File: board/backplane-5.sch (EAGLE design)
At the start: 142 parts, among them CN1 RJ45JACK90, U1 AMS1117-5.0, U10 RT9193, U11 KSZ9897, U12 KSZ8081MLX, U2 AMS1117-5.0, U3 AMS1117-5.0, U4 AMS1117-5.0, U5 AMS1117-5.0, U6 AMS1117-2.5, U7 AMS1117-1.2, U8 RT9193, U9 AMS1117-5.0, X1 25MHz, X2 25MHz

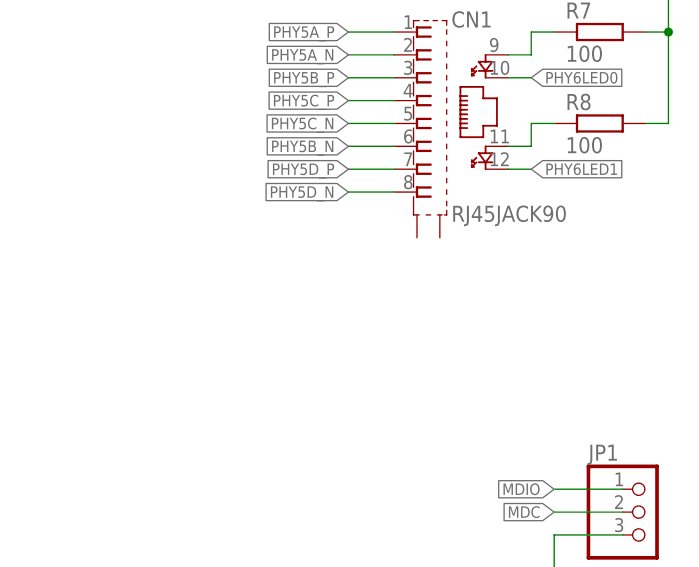
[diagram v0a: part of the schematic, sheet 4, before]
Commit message: Tweaked some packages and placed RPi conn
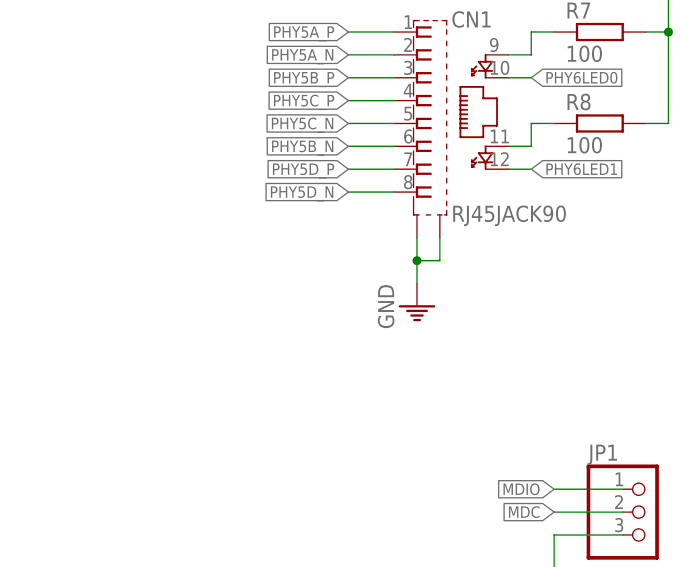
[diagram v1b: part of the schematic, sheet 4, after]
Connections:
- net PE: now also CN1.S1, CN1.S2
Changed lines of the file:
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@@
 <grid distance="0.1" unitdist="inch" unit="inch" style="lines" multiple="1" display="no" altdistance="0.01" altunitdist="inch" altunit="inch"/>
 <layers>
-<layer number="1" name="Top" color="4" fill="1" visible="yes" active="no"/>
-<layer number="2" name="Route2" color="1" fill="3" visible="yes" active="no"/>
-<layer number="3" name="Route3" color="4" fill="3" visible="yes" active="no"/>
-<layer number="4" name="Route4" color="1" fill="4" visible="yes" active="no"/>
-<layer number="5" name="Route5" color="4" fill="4" visible="yes" active="no"/>
-<layer number="6" name="Route6" color="1" fill="8" visible="yes" active="no"/>
-<layer number="7" name="Route7" color="4" fill="8" visible="yes" active="no"/>
-<layer number="8" name="Route8" color="1" fill="2" visible="yes" active="no"/>
-<layer number="9" name="Route9" color="4" fill="2" visible="yes" active="no"/>
-<layer number="10" name="Route10" color="1" fill="7" visible="yes" active="no"/>
-<layer number="11" name="Route11" color="4" fill="7" visible="yes" active="no"/>
-<layer number="12" name="Route12" color="1" fill="5" visible="yes" active="no"/>
-<layer number="13" name="Route13" color="4" fill="5" visible="yes" active="no"/>
-<layer number="14" name="Route14" color="1" fill="6" visible="yes" active="no"/>
-<layer number="15" name="Route15" color="4" fill="6" visible="yes" active="no"/>
-<layer number="16" name="Bottom" color="1" fill="1" visible="yes" active="no"/>
-<layer number="17" name="Pads" color="2" fill="1" visible="yes" active="no"/>
-<layer number="18" name="Vias" color="2" fill="1" visible="yes" active="no"/>
-<layer number="19" name="Unrouted" color="6" fill="1" visible="yes" active="no"/>
-<layer number="20" name="Dimension" color="24" fill="1" visible="yes" active="no"/>
-<layer number="21" name="tPlace" color="7" fill="1" visible="yes" active="no"/>
-<layer number="22" name="bPlace" color="7" fill="1" visible="yes" active="no"/>
-<layer number="23" name="tOrigins" color="15" fill="1" visible="yes" active="no"/>
-<layer number="24" name="bOrigins" color="15" fill="1" visible="yes" active="no"/>
-<layer number="25" name="tNames" color="7" fill="1" visible="yes" active="no"/>
-<layer number="26" name="bNames" color="7" fill="1" visible="yes" active="no"/>
-<layer number="27" name="tValues" color="7" fill="1" visible="yes" active="no"/>
-<layer number="28" name="bValues" color="7" fill="1" visible="yes" active="no"/>
+<layer number="1" name="Top" color="4" fill="1" visible="no" active="no"/>
+<layer number="2" name="Route2" color="1" fill="3" visible="no" active="no"/>
+<layer number="3" name="Route3" color="4" fill="3" visible="no" active="no"/>
+<layer number="4" name="Route4" color="1" fill="4" visible="no" active="no"/>
+<layer number="5" name="Route5" color="4" fill="4" visible="no" active="no"/>
+<layer number="6" name="Route6" color="1" fill="8" visible="no" active="no"/>
+<layer number="7" name="Route7" color="4" fill="8" visible="no" active="no"/>
+<layer number="8" name="Route8" color="1" fill="2" visible="no" active="no"/>
+<layer number="9" name="Route9" color="4" fill="2" visible="no" active="no"/>
+<layer number="10" name="Route10" color="1" fill="7" visible="no" active="no"/>
+<layer number="11" name="Route11" color="4" fill="7" visible="no" active="no"/>
+<layer number="12" name="Route12" color="1" fill="5" visible="no" active="no"/>
+<layer number="13" name="Route13" color="4" fill="5" visible="no" active="no"/>
+<layer number="14" name="Route14" color="1" fill="6" visible="no" active="no"/>
+<layer number="15" name="Route15" color="4" fill="6" visible="no" active="no"/>
+<layer number="16" name="Bottom" color="1" fill="1" visible="no" active="no"/>
+<layer number="17" name="Pads" color="2" fill="1" visible="no" active="no"/>
+<layer number="18" name="Vias" color="2" fill="1" visible="no" active="no"/>
+<layer number="19" name="Unrouted" color="6" fill="1" visible="no" active="no"/>
+<layer number="20" name="Dimension" color="24" fill="1" visible="no" active="no"/>
+<layer number="21" name="tPlace" color="7" fill="1" visible="no" active="no"/>
+<layer number="22" name="bPlace" color="7" fill="1" visible="no" active="no"/>
+<layer number="23" name="tOrigins" color="15" fill="1" visible="no" active="no"/>
+<layer number="24" name="bOrigins" color="15" fill="1" visible="no" active="no"/>
+<layer number="25" name="tNames" color="7" fill="1" visible="no" active="no"/>
+<layer number="26" name="bNames" color="7" fill="1" visible="no" active="no"/>
+<layer number="27" name="tValues" color="7" fill="1" visible="no" active="no"/>
+<layer number="28" name="bValues" color="7" fill="1" visible="no" active="no"/>
 <layer number="29" name="tStop" color="7" fill="3" visible="no" active="no"/>
 <layer number="30" name="bStop" color="7" fill="6" visible="no" active="no"/>
@@
 <layer number="35" name="tGlue" color="7" fill="4" visible="no" active="no"/>
 <layer number="36" name="bGlue" color="7" fill="5" visible="no" active="no"/>
-<layer number="37" name="tTest" color="7" fill="1" visible="yes" active="no"/>
-<layer number="38" name="bTest" color="7" fill="1" visible="yes" active="no"/>
+<layer number="37" name="tTest" color="7" fill="1" visible="no" active="no"/>
+<layer number="38" name="bTest" color="7" fill="1" visible="no" active="no"/>
 <layer number="39" name="tKeepout" color="4" fill="11" visible="no" active="no"/>
 <layer number="40" name="bKeepout" color="1" fill="11" visible="no" active="no"/>
@@
 <layer number="44" name="Drills" color="7" fill="1" visible="no" active="no"/>
 <layer number="45" name="Holes" color="7" fill="1" visible="no" active="no"/>
-<layer number="46" name="Milling" color="3" fill="1" visible="yes" active="no"/>
-<layer number="47" name="Measures" color="7" fill="1" visible="yes" active="no"/>
-<layer number="48" name="Document" color="7" fill="1" visible="yes" active="no"/>
-<layer number="49" name="Reference" color="7" fill="1" visible="yes" active="no"/>
-<layer number="51" name="tDocu" color="7" fill="1" visible="yes" active="no"/>
-<layer number="52" name="bDocu" color="7" fill="1" visible="yes" active="no"/>
+<layer number="46" name="Milling" color="3" fill="1" visible="no" active="no"/>
+<layer number="47" name="Measures" color="7" fill="1" visible="no" active="no"/>
+<layer number="48" name="Document" color="7" fill="1" visible="no" active="no"/>
+<layer number="49" name="Reference" color="7" fill="1" visible="no" active="no"/>
+<layer number="51" name="tDocu" color="7" fill="1" visible="no" active="no"/>
+<layer number="52" name="bDocu" color="7" fill="1" visible="no" active="no"/>
 <layer number="90" name="Modules" color="5" fill="1" visible="yes" active="yes"/>
 <layer number="91" name="Nets" color="2" fill="1" visible="yes" active="yes"/>
@@
 <part name="PE25" library="supply1" library_urn="urn:adsk.eagle:library:371" deviceset="PE" device="" value="GND"/>
 <part name="R32" library="rcl" library_urn="urn:adsk.eagle:library:334" deviceset="R-EU_" device="R0603" package3d_urn="urn:adsk.eagle:package:23555/2" value="1k"/>
+<part name="PE27" library="supply1" library_urn="urn:adsk.eagle:library:371" deviceset="PE" device="" value="GND"/>
 </parts>
 <sheets>
@@
 <instance part="JP1" gate="A" x="241.3" y="91.44"/>
 <instance part="PE25" gate="M" x="231.14" y="81.28"/>
+<instance part="PE27" gate="M" x="215.9" y="114.3"/>
 </instances>
 <busses>
@@
 </segment>
 </net>
+<net name="PE" class="0">
+<segment>
+<pinref part="CN1" gate="P" pin="S1"/>
+<pinref part="PE27" gate="M" pin="PE"/>
+<wire x1="215.9" y1="121.92" x2="215.9" y2="119.38" width="0.1524" layer="91"/>
+<pinref part="CN1" gate="P" pin="S2"/>
+<wire x1="215.9" y1="119.38" x2="215.9" y2="116.84" width="0.1524" layer="91"/>
+<wire x1="218.44" y1="121.92" x2="218.44" y2="119.38" width="0.1524" layer="91"/>
+<wire x1="218.44" y1="119.38" x2="215.9" y2="119.38" width="0.1524" layer="91"/>
+<junction x="215.9" y="119.38"/>
+</segment>
+</net>

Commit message: Fixed led connection
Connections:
- net PHY5LED0: now also CN1.YELLOW_C; no longer R25.2
- net PHY5LED1: now also CN1.GREEN_C; no longer R26.2
- net PHY6LED0: now also R25.2; no longer CN1.YELLOW_C
- net PHY6LED1: now also R26.2; no longer CN1.GREEN_C
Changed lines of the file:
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@@
 <net name="PHY6LED0" class="0">
-<segment>
-<pinref part="CN1" gate="P" pin="YELLOW_C"/>
-<wire x1="226.06" y1="139.7" x2="228.6" y2="139.7" width="0.1524" layer="91"/>
-<label x="228.6" y="139.7" size="1.27" layer="95" xref="yes"/>
-</segment>
 <segment>
 <pinref part="U12" gate="G$1" pin="LED0/NWAYEN"/>
@@
 </net>
 <net name="PHY6LED1" class="0">
-<segment>
-<pinref part="CN1" gate="P" pin="GREEN_C"/>
-<wire x1="226.06" y1="129.54" x2="228.6" y2="129.54" width="0.1524" layer="91"/>
-<label x="228.6" y="129.54" size="1.27" layer="95" xref="yes"/>
-</segment>
 <segment>
 <pinref part="U12" gate="G$1" pin="LED1/SPEED"/>
@@
 <wire x1="218.44" y1="119.38" x2="215.9" y2="119.38" width="0.1524" layer="91"/>
 <junction x="215.9" y="119.38"/>
+</segment>
+</net>
+<net name="PHY5LED0" class="0">
+<segment>
+<pinref part="CN1" gate="P" pin="YELLOW_C"/>
+<wire x1="226.06" y1="139.7" x2="228.6" y2="139.7" width="0.1524" layer="91"/>
+<label x="228.6" y="139.7" size="1.27" layer="95" xref="yes"/>
+</segment>
+</net>
+<net name="PHY5LED1" class="0">
+<segment>
+<pinref part="CN1" gate="P" pin="GREEN_C"/>
+<wire x1="226.06" y1="129.54" x2="228.6" y2="129.54" width="0.1524" layer="91"/>
+<label x="228.6" y="129.54" size="1.27" layer="95" xref="yes"/>
 </segment>
 </net>
@@
 </segment>
 </net>
-<net name="PHY5LED0" class="0">
-<segment>
-<pinref part="R25" gate="G$1" pin="2"/>
-<wire x1="81.28" y1="124.46" x2="81.28" y2="121.92" width="0.1524" layer="91"/>
-<label x="81.28" y="121.92" size="1.27" layer="95" rot="MR270" xref="yes"/>
-</segment>
-</net>
-<net name="PHY5LED1" class="0">
-<segment>
-<pinref part="R26" gate="G$1" pin="2"/>
-<wire x1="88.9" y1="124.46" x2="88.9" y2="121.92" width="0.1524" layer="91"/>
-<label x="88.9" y="121.92" size="1.27" layer="95" rot="MR270" xref="yes"/>
-</segment>
-</net>
 <net name="N$24" class="0">
 <segment>
@@
 </segment>
 </net>
+<net name="PHY6LED0" class="0">
+<segment>
+<pinref part="R25" gate="G$1" pin="2"/>
+<wire x1="81.28" y1="124.46" x2="81.28" y2="121.92" width="0.1524" layer="91"/>
+<label x="81.28" y="121.92" size="1.27" layer="95" rot="MR270" xref="yes"/>
+</segment>
+</net>
+<net name="PHY6LED1" class="0">
+<segment>
+<pinref part="R26" gate="G$1" pin="2"/>
+<wire x1="88.9" y1="124.46" x2="88.9" y2="121.92" width="0.1524" layer="91"/>
+<label x="88.9" y="121.92" size="1.27" layer="95" rot="MR270" xref="yes"/>
+</segment>
+</net>

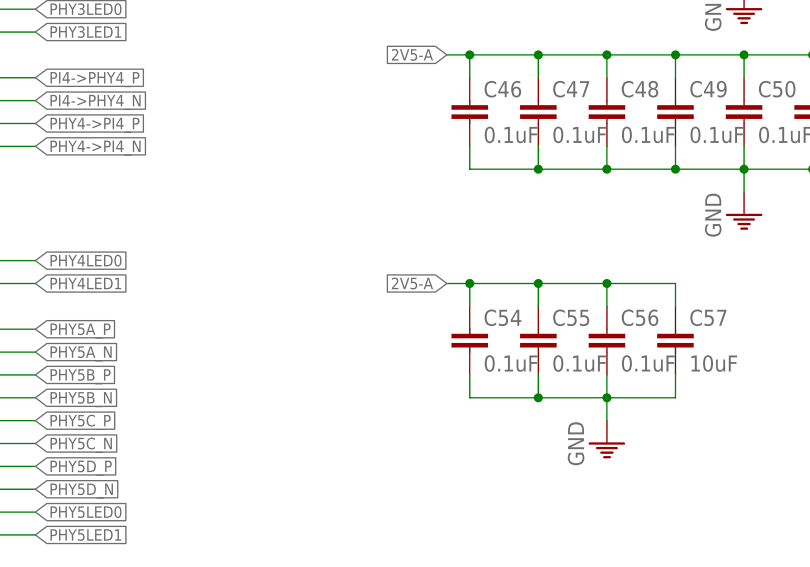
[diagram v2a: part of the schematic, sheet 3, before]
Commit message: Fixed some errors due to ground on the schematic
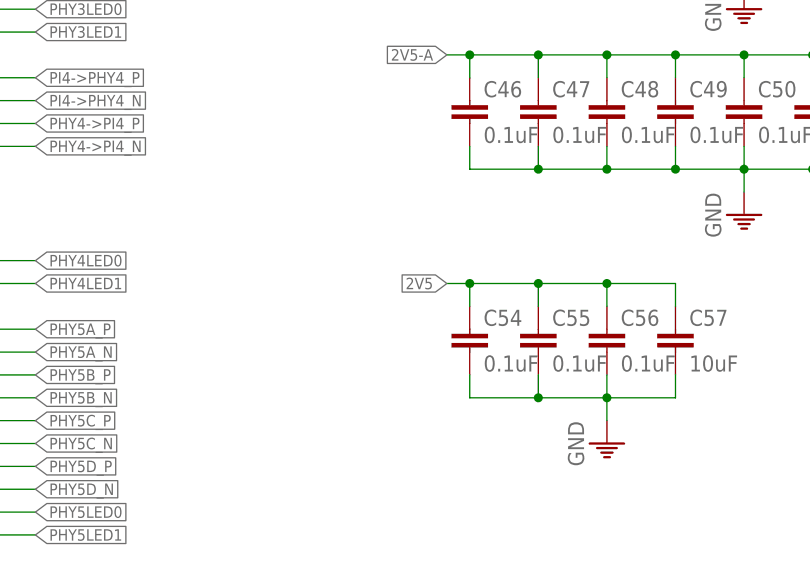
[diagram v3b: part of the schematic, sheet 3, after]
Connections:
- removed net PE: C23.2, C24.2, C27.2, C28.2, C29.2, C30.2, C31.2, C32.2, C33.2, C34.2, C35.2, C36.2, C37.2, C38.2, C39.2, C40.2, C41.2, C42.2, C43.2, C44.2, C45.2, C46.2, C47.2, C48.2, C49.2, C50.2, C51.2, C52.2, C53.2, C54.2, C55.2, C56.2, C57.2, CN1.S1, CN1.S2
- net 2V5: now also C54.1, C55.1, C56.1, C57.1
- net 2V5-A: no longer C54.1, C55.1, C56.1, C57.1
- net GND: now also C23.2, C24.2, C27.2, C28.2, C29.2, C30.2, C31.2, C32.2, C33.2, C34.2, C35.2, C36.2, C37.2, C38.2, C39.2, C40.2, C41.2, C42.2, C43.2, C44.2, C45.2, C46.2, C47.2, C48.2, C49.2, C50.2, C51.2, C52.2, C53.2, C54.2, C55.2, C56.2, C57.2, CN1.S1, CN1.S2

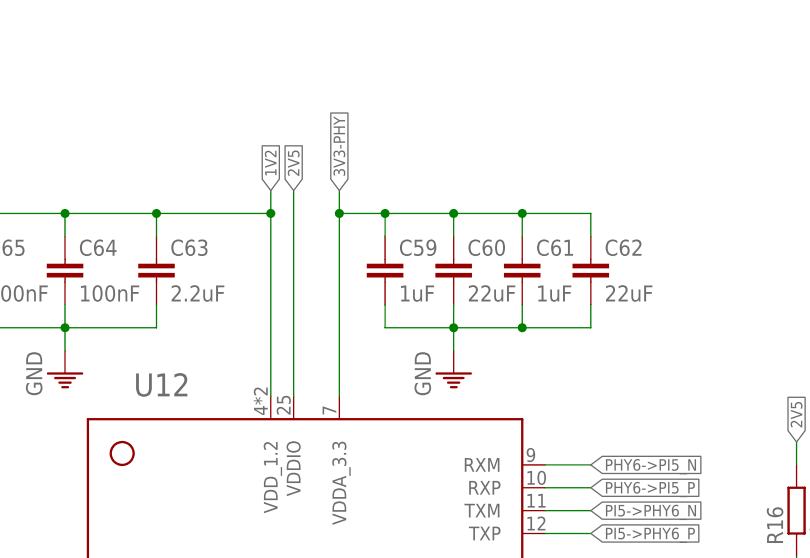
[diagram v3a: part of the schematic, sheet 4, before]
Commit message: Fix decoupling for the PHY
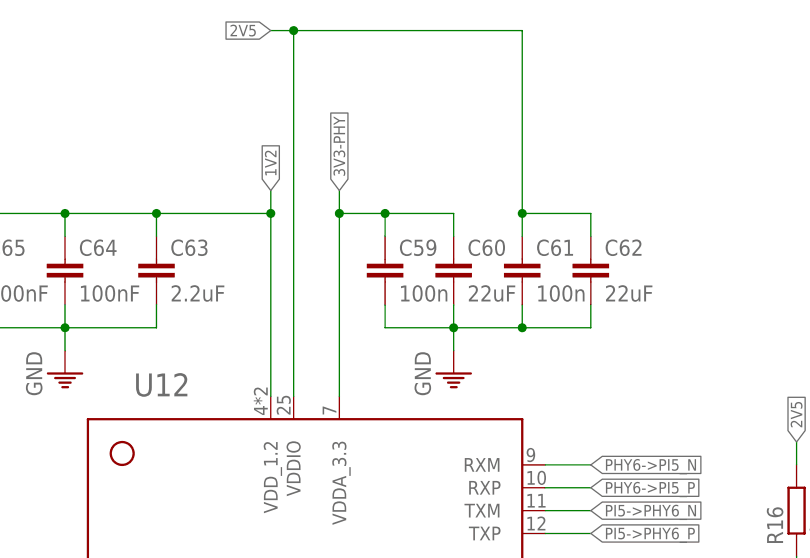
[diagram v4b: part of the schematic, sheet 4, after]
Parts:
- C59, C61: value 1uF -> 100n
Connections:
- net 2V5: now also C61.1, C62.1
- net 3V3-PHY: no longer C61.1, C62.1
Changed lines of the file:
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@@
 <?xml version="1.0" encoding="utf-8"?>
 <!DOCTYPE eagle SYSTEM "eagle.dtd">
-<eagle version="8.3.1">
+<eagle version="8.3.2">
 <drawing>
 <settings>
@@
 <part name="U12" library="tuetuopay" deviceset="KSZ8081MLX" device=""/>
 <part name="PE15" library="supply1" library_urn="urn:adsk.eagle:library:371" deviceset="PE" device="" value="GND"/>
-<part name="C59" library="tuetuopay" deviceset="C" device="0603" value="1uF"/>
+<part name="C59" library="tuetuopay" deviceset="C" device="0603" value="100n"/>
 <part name="C60" library="tuetuopay" deviceset="C" device="0603" value="22uF"/>
 <part name="PE16" library="supply1" library_urn="urn:adsk.eagle:library:371" deviceset="PE" device="" value="GND"/>
-<part name="C61" library="tuetuopay" deviceset="C" device="0603" value="1uF"/>
+<part name="C61" library="tuetuopay" deviceset="C" device="0603" value="100n"/>
 <part name="C62" library="tuetuopay" deviceset="C" device="0603" value="22uF"/>
 <part name="C63" library="tuetuopay" deviceset="C" device="0603" value="2.2uF"/>
@@
 <junction x="93.98" y="147.32"/>
 <label x="93.98" y="149.86" size="1.27" layer="95" rot="R90" xref="yes"/>
-<pinref part="C61" gate="&gt;NAME" pin="1"/>
-<wire x1="106.68" y1="147.32" x2="114.3" y2="147.32" width="0.1524" layer="91"/>
-<wire x1="114.3" y1="147.32" x2="114.3" y2="144.78" width="0.1524" layer="91"/>
-<junction x="106.68" y="147.32"/>
-<pinref part="C62" gate="&gt;NAME" pin="1"/>
-<wire x1="114.3" y1="147.32" x2="121.92" y2="147.32" width="0.1524" layer="91"/>
-<wire x1="121.92" y1="147.32" x2="121.92" y2="144.78" width="0.1524" layer="91"/>
-<junction x="114.3" y="147.32"/>
 </segment>
 <segment>
@@
 <segment>
 <pinref part="U12" gate="G$1" pin="VDDIO"/>
-<wire x1="88.9" y1="127" x2="88.9" y2="149.86" width="0.1524" layer="91"/>
-<label x="88.9" y="149.86" size="1.27" layer="95" rot="R90" xref="yes"/>
-</segment>
-<segment>
+<wire x1="88.9" y1="127" x2="88.9" y2="167.64" width="0.1524" layer="91"/>
+<wire x1="88.9" y1="167.64" x2="86.36" y2="167.64" width="0.1524" layer="91"/>
+<label x="86.36" y="167.64" size="1.27" layer="95" rot="R180" xref="yes"/>
+<pinref part="C61" gate="&gt;NAME" pin="1"/>
+<pinref part="C62" gate="&gt;NAME" pin="1"/>
+<wire x1="121.92" y1="147.32" x2="121.92" y2="144.78" width="0.1524" layer="91"/>
+<wire x1="114.3" y1="147.32" x2="121.92" y2="147.32" width="0.1524" layer="91"/>
+<wire x1="114.3" y1="147.32" x2="114.3" y2="144.78" width="0.1524" layer="91"/>
+<wire x1="88.9" y1="167.64" x2="114.3" y2="167.64" width="0.1524" layer="91"/>
+<wire x1="114.3" y1="167.64" x2="114.3" y2="147.32" width="0.1524" layer="91"/>
+<junction x="88.9" y="167.64"/>
+<junction x="114.3" y="147.32"/>
+</segment>
+<segment>

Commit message: Added STM32F217
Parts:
- added U13: STM32F217-100, tuetuopay:STM32F217-100
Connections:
- net 3V3-LED renamed 3V3-STM32
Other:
- note added: "STM32"
- note removed: "LEDs"
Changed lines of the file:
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@@
 <part name="R32" library="rcl" library_urn="urn:adsk.eagle:library:334" deviceset="R-EU_" device="R0603" package3d_urn="urn:adsk.eagle:package:23555/2" value="1k"/>
 <part name="PE27" library="supply1" library_urn="urn:adsk.eagle:library:371" deviceset="PE" device="" value="GND"/>
+<part name="FRAME6" library="frames" library_urn="urn:adsk.eagle:library:229" deviceset="A4L-LOC" device=""/>
+<part name="U13" library="tuetuopay" deviceset="STM32F217-100" device=""/>
 </parts>
 <sheets>
@@
 <text x="106.68" y="165.1" size="1.778" layer="90">Switch</text>
 <text x="106.68" y="86.36" size="1.778" layer="90">Misc</text>
-<text x="193.04" y="127" size="1.778" layer="90">LEDs</text>
+<text x="193.04" y="127" size="1.778" layer="90">STM32</text>
 <text x="193.04" y="71.12" size="1.778" layer="90">PHY</text>
 </plain>
@@
 </segment>
 </net>
-<net name="3V3-LED" class="0">
+<net name="3V3-STM32" class="0">
 <segment>
 <pinref part="U8" gate="G$1" pin="VOUT"/>
@@
 </nets>
 </sheet>
+<sheet>
+<plain>
+<text x="218.44" y="20.32" size="2.54" layer="90">STM32</text>
+</plain>
+<instances>
+<instance part="FRAME6" gate="G$1" x="0" y="0"/>
+<instance part="U13" gate="G$1" x="109.22" y="91.44"/>
+</instances>
+<busses>
+</busses>
+<nets>
+</nets>
+</sheet>
